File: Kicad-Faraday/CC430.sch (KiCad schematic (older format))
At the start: 33 parts, among them P2 DNP, U1 CC430F6137, U14 0915BM15A0001E, X1 ST3215SB32768H5HPWAA, X2 ABM8G-26.000MHZ-18-D2Y-T

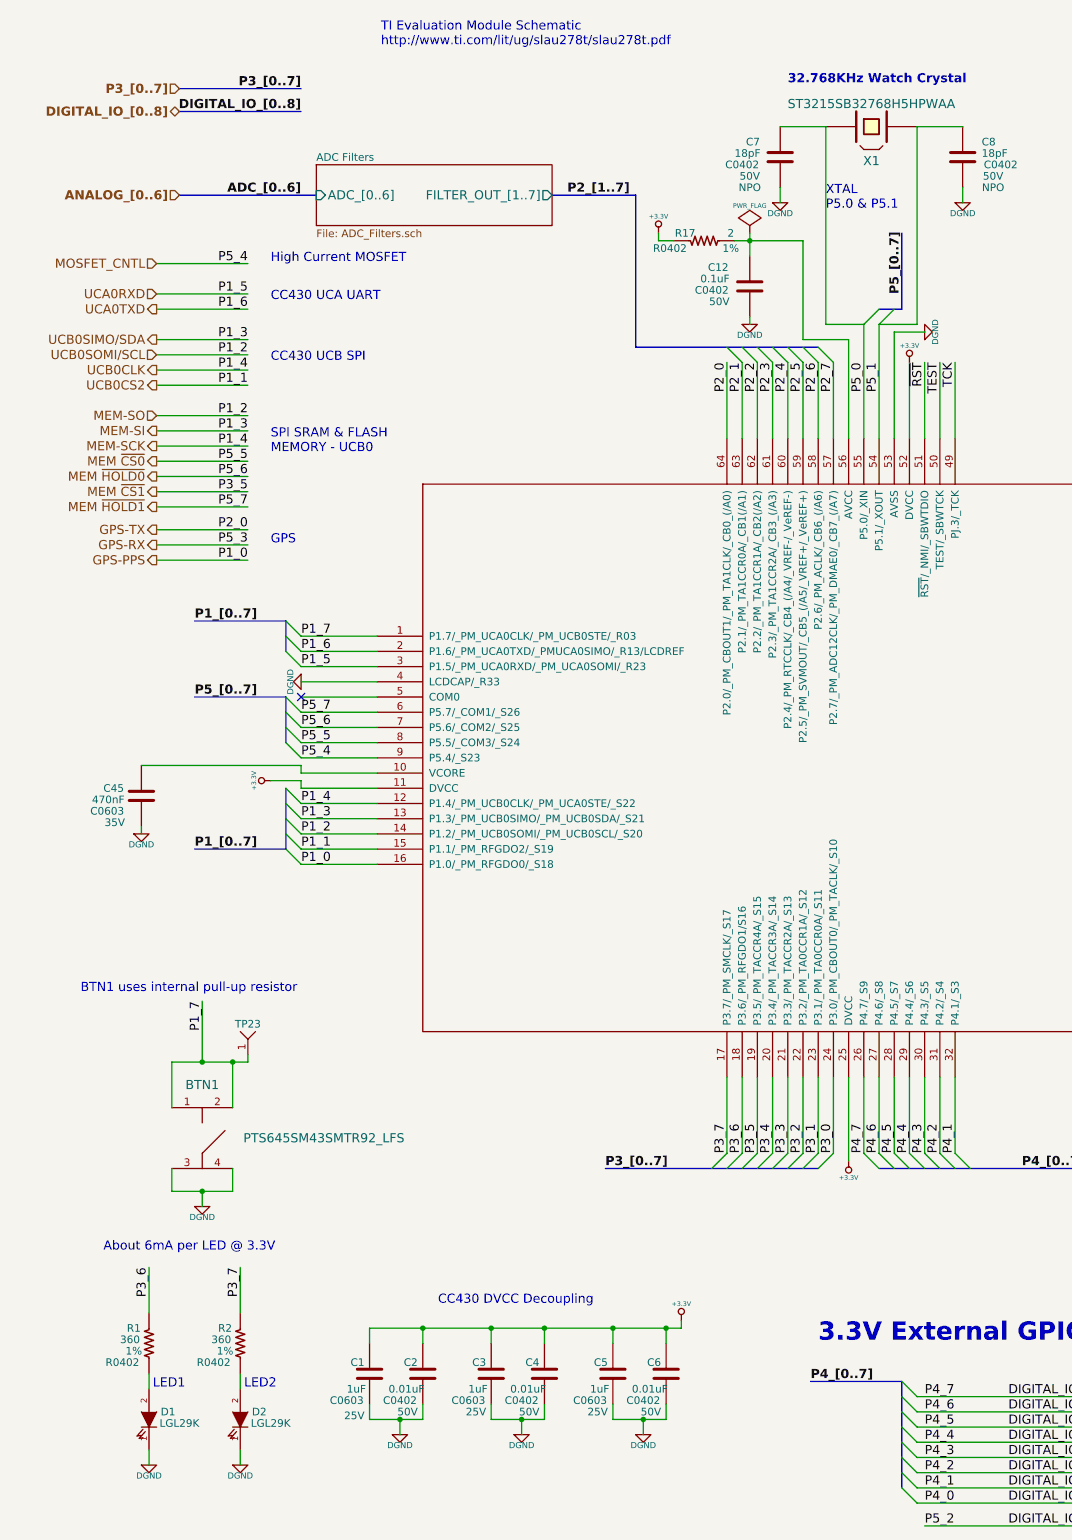
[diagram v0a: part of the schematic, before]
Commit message: Updated BOM .csv and added a REV C BOM Excel document as well as Rev C ICD Excel document. Updated PCB layout file to include P3 and P4 swaps for GD0 changes per GitHub Hardware IT #6.
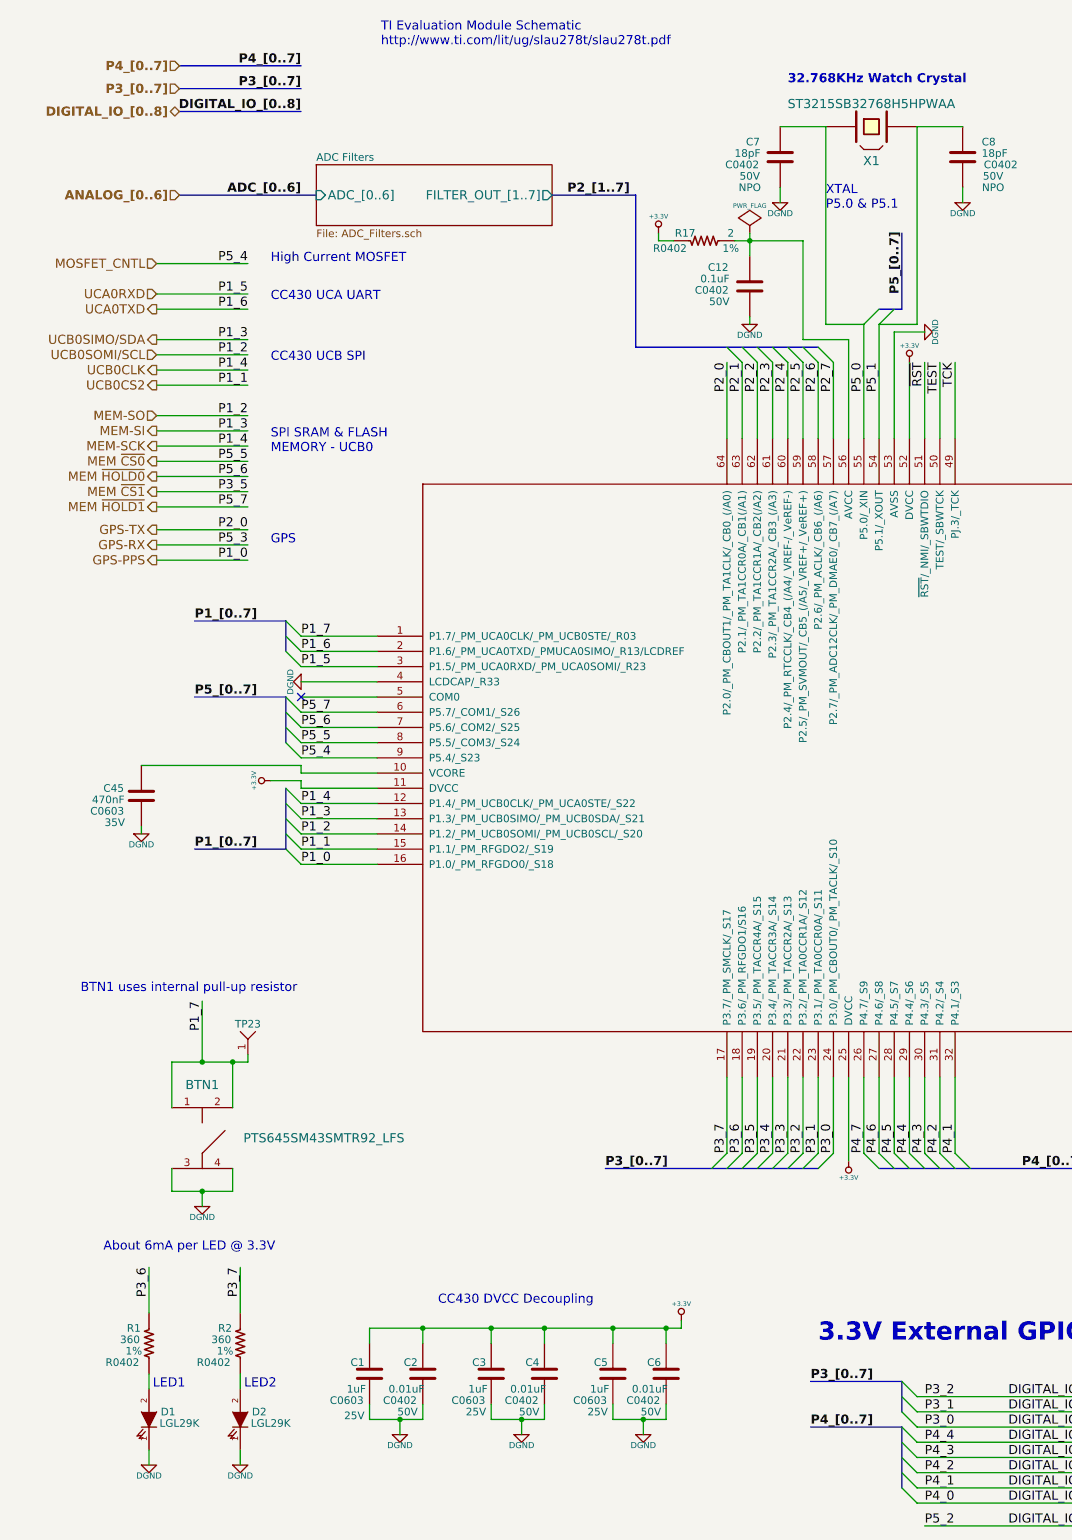
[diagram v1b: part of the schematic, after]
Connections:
- net P3_0 is gone; now on net DIGITAL_IO_2: U1.24 (P3.0/_PM_CBOUT0/_PM_TACLK/_S10)
- net P3_1 is gone; now on net DIGITAL_IO_1: U1.23 (P3.1/_PM_TA0CCR0A/_S11)
- net P3_2 is gone; now on net DIGITAL_IO_0: U1.22 (P3.2/_PM_TA0CCR1A/_S12)
- net DIGITAL_IO_0: no longer U1.26 (P4.7/_S9)
- net DIGITAL_IO_1: no longer U1.27 (P4.6/_S8)
- net DIGITAL_IO_2: no longer U1.28 (P4.5/_S7)
- new net P4_5: U1.28 (P4.5/_S7)
- new net P4_6: U1.27 (P4.6/_S8)
- new net P4_7: U1.26 (P4.7/_S9)
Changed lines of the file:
@@
 	1    0    0    -1
 $EndComp
-Text Label 5600 9450 0    60   ~ 12
+Text Label 5600 9750 0    60   ~ 12
 P4_[0..7]
 Text Notes 5650 9200 0    120  ~ 24
@@
 56 10 04 A1 18 0C 2B 08 82 50 0C 86 15 04 41 28 06 C3 0A 82 20 14 83 61 05 41 10 8A C1 B0 82 20
 08 C5 60 58 41 10 84 62 30 AC 20 08 42 31 FF 0F 83 E1 BA 3C 1C 59 E8 E4 00 00 00 00 49 45 4E 44
-AE 42 60 82 4D $EndBitmap
+AE 42 60 82 17 $EndBitmap
 EndData
 $EndBitmap
@@
 DIGITAL_IO_8
 Wire Bus Line
-	5600 9450 6200 9450
-Wire Bus Line
-	6200 9450 6200 10150
+	5600 9750 6200 9750
 Wire Wire Line
 	6300 9550 7500 9550
@@
 P4_4
 Text Label 6350 9750 0    60   ~ 0
-P4_5
+P3_0
 Text Label 6350 9650 0    60   ~ 0
-P4_6
+P3_1
 Text Label 6350 9550 0    60   ~ 0
-P4_7
+P3_2
 Text Label 1900 3700 2    60   ~ 0
 P5_7
@@
 	0    1    1    0
 $EndComp
+Wire Bus Line
+	6200 9750 6200 10150
+Text Label 5600 9450 0    60   ~ 12
+P3_[0..7]
+Wire Bus Line
+	5600 9450 6200 9450
+Wire Bus Line
+	6200 9450 6200 9650
+Text Label 2250 800  2    60   ~ 12
+P4_[0..7]
+Wire Bus Line
+	1450 800  2250 800
+Text HLabel 1450 800  0    60   Input ~ 12
+P4_[0..7]
 $EndSCHEMATC

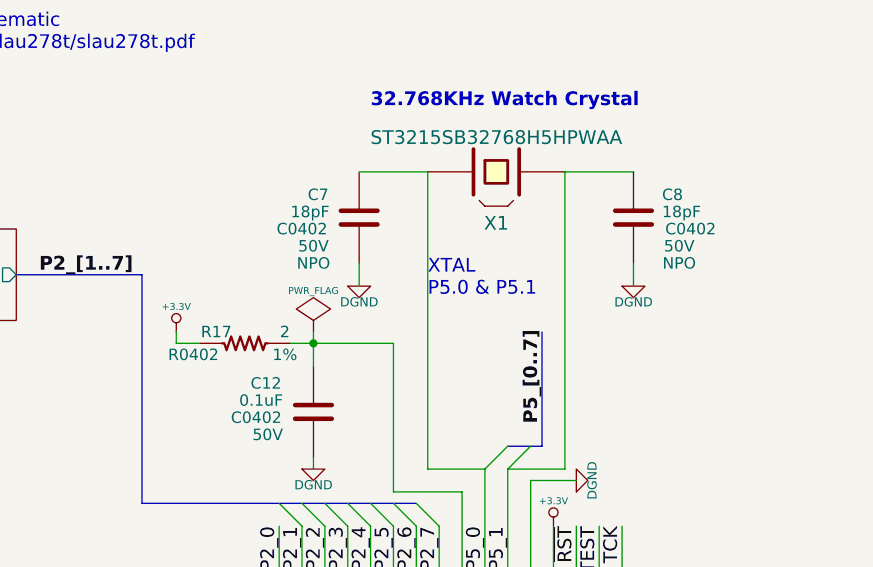
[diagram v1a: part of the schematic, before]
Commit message: Updated per RevD Github Issue comments. Largely removed unnecessary items
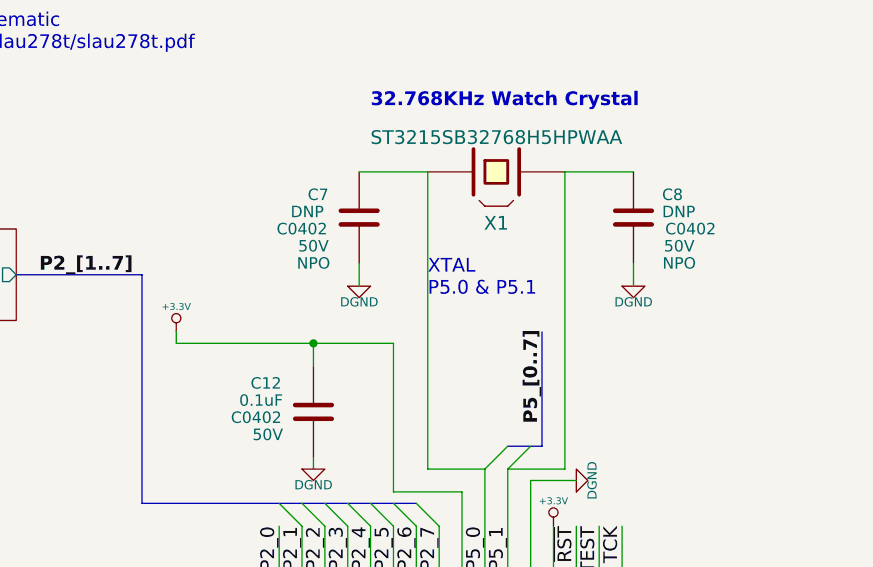
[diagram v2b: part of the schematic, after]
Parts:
- removed R17: 2, R0402, symbol R_US
- C7, C8: value 18pF -> DNP
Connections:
- net +3.3V: now also C12.1, U1.56 (AVCC)
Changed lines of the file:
@@
 Sheet 3 11
 Title "Faraday Wireless Node"
-Date "24 oct 2016"
+Date "10 nov 2016"
 Rev "C"
 Comp "FaradayRF"
@@
 P 6600 1400
 F 0 "C8" H 6725 1500 50  0000 L CNN
-F 1 "18pF" H 6725 1425 50  0000 L CNN
+F 1 "DNP" H 6725 1425 50  0000 L CNN
 F 2 "C0402" H 6850 1350 50  0000 C CNN
 F 3 "" H 6600 1400 60  0000 C CNN
@@
 P 5400 1400
 F 0 "C7" H 5175 1500 50  0000 L CNN
-F 1 "18pF" H 5100 1425 50  0000 L CNN
+F 1 "DNP" H 5100 1425 50  0000 L CNN
 F 2 "C0402" H 5150 1350 50  0000 C CNN
 F 3 "" H 5400 1400 60  0000 C CNN
@@
 NoConn ~ 10700 1950
 $Comp
-L PWR_FLAG #FLG019
+L PWR_FLAG #FLG014
 U 1 1 5416AA97
 P 12250 3400
-F 0 "#FLG019" H 12250 3495 30  0001 C CNN
+F 0 "#FLG014" H 12250 3495 30  0001 C CNN
 F 1 "PWR_FLAG" H 12250 3580 30  0000 C CNN
 F 2 "" H 12250 3400 60  0000 C CNN
@@
 P2_[1..7]
 $Comp
-L +3.3V #PWR020
+L +3.3V #PWR015
 U 1 1 54FE8D21
 P 6250 2750
-F 0 "#PWR020" H 6250 2710 30  0001 C CNN
+F 0 "#PWR015" H 6250 2710 30  0001 C CNN
 F 1 "+3.3V" H 6250 2860 30  0000 C CNN
 F 2 "" H 6250 2750 60  0000 C CNN
@@
 $EndComp
 $Comp
-L +3.3V #PWR021
+L +3.3V #PWR016
 U 1 1 54FE8D46
 P 5850 8000
-F 0 "#PWR021" H 5850 7960 30  0001 C CNN
+F 0 "#PWR016" H 5850 7960 30  0001 C CNN
 F 1 "+3.3V" H 5850 8110 30  0000 C CNN
 F 2 "" H 5850 8000 60  0000 C CNN
@@
 $EndComp
 $Comp
-L +3.3V #PWR022
+L +3.3V #PWR017
 U 1 1 54FE8D77
 P 4750 9050
-F 0 "#PWR022" H 4750 9010 30  0001 C CNN
+F 0 "#PWR017" H 4750 9010 30  0001 C CNN
 F 1 "+3.3V" H 4750 9160 30  0000 C CNN
 F 2 "" H 4750 9050 60  0000 C CNN
@@
 $EndComp
 $Comp
-L +3.3V #PWR023
+L +3.3V #PWR018
 U 1 1 54FE8D9C
 P 2050 5500
-F 0 "#PWR023" H 2050 5460 30  0001 C CNN
+F 0 "#PWR018" H 2050 5460 30  0001 C CNN
 F 1 "+3.3V" H 2050 5610 30  0000 C CNN
 F 2 "" H 2050 5500 60  0000 C CNN
@@
 $EndComp
 $Comp
-L +3.3V #PWR024
+L +3.3V #PWR019
 U 1 1 54FE8DCD
 P 13200 1350
-F 0 "#PWR024" H 13200 1310 30  0001 C CNN
+F 0 "#PWR019" H 13200 1310 30  0001 C CNN
 F 1 "+3.3V" H 13200 1460 30  0000 C CNN
 F 2 "" H 13200 1350 60  0000 C CNN
@@
 $EndComp
 $Comp
-L +3.3V #PWR025
+L +3.3V #PWR020
 U 1 1 54FE8DF2
 P 10050 1350
-F 0 "#PWR025" H 10050 1310 30  0001 C CNN
+F 0 "#PWR020" H 10050 1310 30  0001 C CNN
 F 1 "+3.3V" H 10050 1460 30  0000 C CNN
 F 2 "" H 10050 1350 60  0000 C CNN
@@
 $EndComp
 $Comp
-L +3.3V #PWR026
+L +3.3V #PWR021
 U 1 1 54FE8E1D
 P 4600 1900
-F 0 "#PWR026" H 4600 1860 30  0001 C CNN
+F 0 "#PWR021" H 4600 1860 30  0001 C CNN
 F 1 "+3.3V" H 4600 2010 30  0000 C CNN
 F 2 "" H 4600 1900 60  0000 C CNN
@@
 $EndComp
 $Comp
-L +3.3V #PWR027
+L +3.3V #PWR022
 U 1 1 54FE8E42
 P 13250 3450
-F 0 "#PWR027" H 13250 3410 30  0001 C CNN
+F 0 "#PWR022" H 13250 3410 30  0001 C CNN
 F 1 "+3.3V" H 13250 3560 30  0000 C CNN
 F 2 "" H 13250 3450 60  0000 C CNN
@@
 RF-PWR
 $Comp
-L DGND #PWR028
+L DGND #PWR023
 U 1 1 5518037B
 P 5400 1700
-F 0 "#PWR028" H 5400 1700 40  0001 C CNN
+F 0 "#PWR023" H 5400 1700 40  0001 C CNN
 F 1 "DGND" H 5400 1630 40  0000 C CNN
 F 2 "~" H 5400 1700 60  0000 C CNN
@@
 $EndComp
 $Comp
-L DGND #PWR029
+L DGND #PWR024
 U 1 1 55180450
 P 6600 1700
-F 0 "#PWR029" H 6600 1700 40  0001 C CNN
+F 0 "#PWR024" H 6600 1700 40  0001 C CNN
 F 1 "DGND" H 6600 1630 40  0000 C CNN
 F 2 "~" H 6600 1700 60  0000 C CNN
@@
 $EndComp
 $Comp
-L DGND #PWR030
+L DGND #PWR025
 U 1 1 551805A0
 P 12700 1800
-F 0 "#PWR030" H 12700 1800 40  0001 C CNN
+F 0 "#PWR025" H 12700 1800 40  0001 C CNN
 F 1 "DGND" H 12700 1730 40  0000 C CNN
 F 2 "~" H 12700 1800 60  0000 C CNN
@@
 $EndComp
 $Comp
-L DGND #PWR031
+L DGND #PWR026
 U 1 1 551805D3
 P 13200 2550
-F 0 "#PWR031" H 13200 2550 40  0001 C CNN
+F 0 "#PWR026" H 13200 2550 40  0001 C CNN
 F 1 "DGND" H 13200 2480 40  0000 C CNN
 F 2 "~" H 13200 2550 60  0000 C CNN
@@
 $EndComp
 $Comp
-L DGND #PWR032
+L DGND #PWR027
 U 1 1 55180832
 P 9450 9600
-F 0 "#PWR032" H 9450 9600 40  0001 C CNN
+F 0 "#PWR027" H 9450 9600 40  0001 C CNN
 F 1 "DGND" H 9450 9530 40  0000 C CNN
 F 2 "~" H 9450 9600 60  0000 C CNN
@@
 $EndComp
 $Comp
-L DGND #PWR033
+L DGND #PWR028
 U 1 1 55180838
 P 10050 9600
-F 0 "#PWR033" H 10050 9600 40  0001 C CNN
+F 0 "#PWR028" H 10050 9600 40  0001 C CNN
 F 1 "DGND" H 10050 9530 40  0000 C CNN
 F 2 "~" H 10050 9600 60  0000 C CNN
@@
 $EndComp
 $Comp
-L DGND #PWR034
+L DGND #PWR029
 U 1 1 551809BC
 P 8950 7150
-F 0 "#PWR034" H 8950 7150 40  0001 C CNN
+F 0 "#PWR029" H 8950 7150 40  0001 C CNN
 F 1 "DGND" H 8950 7080 40  0000 C CNN
 F 2 "~" H 8950 7150 60  0000 C CNN
@@
 $EndComp
 $Comp
-L DGND #PWR035
+L DGND #PWR030
 U 1 1 55180BC3
 P 1200 5850
-F 0 "#PWR035" H 1200 5850 40  0001 C CNN
+F 0 "#PWR030" H 1200 5850 40  0001 C CNN
 F 1 "DGND" H 1200 5780 40  0000 C CNN
 F 2 "~" H 1200 5850 60  0000 C CNN
@@
 $EndComp
 $Comp
-L DGND #PWR036
+L DGND #PWR031
 U 1 1 55180C86
 P 1600 8300
-F 0 "#PWR036" H 1600 8300 40  0001 C CNN
+F 0 "#PWR031" H 1600 8300 40  0001 C CNN
 F 1 "DGND" H 1600 8230 40  0000 C CNN
 F 2 "~" H 1600 8300 60  0000 C CNN
@@
 $EndComp
 $Comp
-L DGND #PWR037
+L DGND #PWR032
 U 1 1 55180D37
 P 1850 10000
-F 0 "#PWR037" H 1850 10000 40  0001 C CNN
+F 0 "#PWR032" H 1850 10000 40  0001 C CNN
 F 1 "DGND" H 1850 9930 40  0000 C CNN
 F 2 "~" H 1850 10000 60  0000 C CNN
@@
 $EndComp
 $Comp
-L DGND #PWR038
+L DGND #PWR033
 U 1 1 55180D58
 P 1250 10000
-F 0 "#PWR038" H 1250 10000 40  0001 C CNN
+F 0 "#PWR033" H 1250 10000 40  0001 C CNN
 F 1 "DGND" H 1250 9930 40  0000 C CNN
 F 2 "~" H 1250 10000 60  0000 C CNN
@@
 $EndComp
 $Comp
-L DGND #PWR039
+L DGND #PWR034
 U 1 1 55180ED9
 P 2900 9800
-F 0 "#PWR039" H 2900 9800 40  0001 C CNN
+F 0 "#PWR034" H 2900 9800 40  0001 C CNN
 F 1 "DGND" H 2900 9730 40  0000 C CNN
 F 2 "~" H 2900 9800 60  0000 C CNN
@@
 $EndComp
 $Comp
-L DGND #PWR040
+L DGND #PWR035
 U 1 1 55180EE6
 P 3700 9800
-F 0 "#PWR040" H 3700 9800 40  0001 C CNN
+F 0 "#PWR035" H 3700 9800 40  0001 C CNN
 F 1 "DGND" H 3700 9730 40  0000 C CNN
 F 2 "~" H 3700 9800 60  0000 C CNN
@@
 $EndComp
 $Comp
-L DGND #PWR041
+L DGND #PWR036
 U 1 1 55180EEC
 P 4500 9800
-F 0 "#PWR041" H 4500 9800 40  0001 C CNN
+F 0 "#PWR036" H 4500 9800 40  0001 C CNN
 F 1 "DGND" H 4500 9730 40  0000 C CNN
 F 2 "~" H 4500 9800 60  0000 C CNN
@@
 $EndComp
 $Comp
-L DGND #PWR042
+L DGND #PWR037
 U 1 1 55183E70
 P 9750 9000
-F 0 "#PWR042" H 9750 9000 40  0001 C CNN
+F 0 "#PWR037" H 9750 9000 40  0001 C CNN
 F 1 "DGND" H 9750 8930 40  0000 C CNN
 F 2 "~" H 9750 9000 60  0000 C CNN
@@
 32.768KHz Watch Crystal
 $Comp
-L DGND #PWR043
+L DGND #PWR038
 U 1 1 55A542F7
 P 11450 4250
-F 0 "#PWR043" H 11450 4250 40  0001 C CNN
+F 0 "#PWR038" H 11450 4250 40  0001 C CNN
 F 1 "DGND" H 11450 4180 40  0000 C CNN
 F 2 "~" H 11450 4250 60  0000 C CNN
@@
 $EndComp
 $Comp
-L DGND #PWR044
+L DGND #PWR039
 U 1 1 55A543D5
 P 10450 4250
-F 0 "#PWR044" H 10450 4250 40  0001 C CNN
+F 0 "#PWR039" H 10450 4250 40  0001 C CNN
 F 1 "DGND" H 10450 4180 40  0000 C CNN
 F 2 "~" H 10450 4250 60  0000 C CNN
@@
 $EndComp
 $Comp
-L DGND #PWR045
+L DGND #PWR040
 U 1 1 55A54975
 P 9850 5000
-F 0 "#PWR045" H 9850 5000 40  0001 C CNN
+F 0 "#PWR040" H 9850 5000 40  0001 C CNN
 F 1 "DGND" H 9850 4930 40  0000 C CNN
 F 2 "~" H 9850 5000 60  0000 C CNN
@@
 $EndComp
 $Comp
-L DGND #PWR046
+L DGND #PWR041
 U 1 1 55BDE204
 P 6350 2550
-F 0 "#PWR046" H 6350 2550 40  0001 C CNN
+F 0 "#PWR041" H 6350 2550 40  0001 C CNN
 F 1 "DGND" H 6350 2480 40  0000 C CNN
 F 2 "~" H 6350 2550 60  0000 C CNN
@@
 $EndComp
 $Comp
-L DGND #PWR047
+L DGND #PWR042
 U 1 1 55BDE222
 P 5200 2500
-F 0 "#PWR047" H 5200 2500 40  0001 C CNN
+F 0 "#PWR042" H 5200 2500 40  0001 C CNN
 F 1 "DGND" H 5200 2430 40  0000 C CNN
 F 2 "~" H 5200 2500 60  0000 C CNN
@@
 	1    0    0    -1
 $EndComp
-$Comp
-L R_US R17
-U 1 1 55BF5F34
-P 4900 1950
-F 0 "R17" V 4950 2075 50  0000 C CNN
-F 1 "2" V 4950 1775 50  0000 C CNN
-F 2 "R0402" V 4850 2175 50  0000 C CNN
-F 3 "" H 4900 1950 60  0000 C CNN
-F 4 "1%" V 4850 1775 50  0000 C CNN "Tolerance"
-	1    4900 1950
-	0    -1   -1   0
-$EndComp
 Text Notes 12450 3700 0    60   ~ 0
 Ferrite Bead
-$Comp
-L PWR_FLAG #FLG048
-U 1 1 55C2C142
-P 5200 1900
-F 0 "#FLG048" H 5200 1995 30  0001 C CNN
-F 1 "PWR_FLAG" H 5200 2080 30  0000 C CNN
-F 2 "" H 5200 1900 60  0000 C CNN
-F 3 "" H 5200 1900 60  0000 C CNN
-	1    5200 1900
-	1    0    0    -1
-$EndComp
 $Bitmap
 Pos 1300 6400
@@
 56 10 04 A1 18 0C 2B 08 82 50 0C 86 15 04 41 28 06 C3 0A 82 20 14 83 61 05 41 10 8A C1 B0 82 20
 08 C5 60 58 41 10 84 62 30 AC 20 08 42 31 FF 0F 83 E1 BA 3C 1C 59 E8 E4 00 00 00 00 49 45 4E 44
-AE 42 60 82 17 $EndBitmap
+AE 42 60 82 33 $EndBitmap
 EndData
 $EndBitmap
 $Comp
-L DGND #PWR049
+L DGND #PWR043
 U 1 1 55C4A709
 P 2250 4850
-F 0 "#PWR049" H 2250 4850 40  0001 C CNN
+F 0 "#PWR043" H 2250 4850 40  0001 C CNN
 F 1 "DGND" H 2250 4780 40  0000 C CNN
 F 2 "~" H 2250 4850 60  0000 C CNN
@@
 Connection ~ 5200 1950
 Wire Wire Line
-	5100 1950 5550 1950
-Wire Wire Line
-	4600 1950 4700 1950
+	4600 1950 5550 1950
 Wire Wire Line
 	4600 1900 4600 1950
@@
 Wire Wire Line
 	5200 2450 5200 2500
-Wire Wire Line
-	5200 1900 5200 2050
 Connection ~ 1600 7350
 Wire Wire Line
@@
 Connection ~ 10300 1650
 $Comp
-L DGND #PWR050
+L DGND #PWR044
 U 1 1 578D5F78
 P 10300 2550
-F 0 "#PWR050" H 10300 2550 40  0001 C CNN
+F 0 "#PWR044" H 10300 2550 40  0001 C CNN
 F 1 "DGND" H 10300 2480 40  0000 C CNN
 F 2 "~" H 10300 2550 60  0000 C CNN
@@
 	10350 5750 10400 5750
 $Comp
-L DGND #PWR051
+L DGND #PWR045
 U 1 1 57944E95
 P 11700 6350
-F 0 "#PWR051" H 11700 6350 40  0001 C CNN
+F 0 "#PWR045" H 11700 6350 40  0001 C CNN
 F 1 "DGND" H 11700 6280 40  0000 C CNN
 F 2 "~" H 11700 6350 60  0000 C CNN
@@
 Text HLabel 1450 800  0    60   Input ~ 12
 P4_[0..7]
+Wire Wire Line
+	5200 1950 5200 2050
 $EndSCHEMATC

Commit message: Saving current RevD, need ot export BOM
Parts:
- BTN1: value PTS645SM43SMTR92_LFS -> DNP
- C2, C4, C6: value 0.01uF -> 0.1uF
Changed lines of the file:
@@
 P 3050 9400
 F 0 "C2" H 2925 9475 50  0000 L CNN
-F 1 "0.01uF" H 2825 9300 50  0000 L CNN
+F 1 "0.1uF" H 2825 9300 50  0000 L CNN
 F 2 "C0402" H 2900 9225 50  0000 C CNN
 F 3 "" H 3050 9400 60  0000 C CNN
@@
 P 3850 9400
 F 0 "C4" H 3725 9475 50  0000 L CNN
-F 1 "0.01uF" H 3625 9300 50  0000 L CNN
+F 1 "0.1uF" H 3625 9300 50  0000 L CNN
 F 2 "C0402" H 3700 9225 50  0000 C CNN
 F 3 "" H 3850 9400 60  0000 C CNN
@@
 P 4650 9400
 F 0 "C6" H 4525 9475 50  0000 L CNN
-F 1 "0.01uF" H 4425 9300 50  0000 L CNN
+F 1 "0.1uF" H 4425 9300 50  0000 L CNN
 F 2 "C0402" H 4500 9225 50  0000 C CNN
 F 3 "" H 4650 9400 60  0000 C CNN
@@
 P 1600 7850
 F 0 "BTN1" H 1600 8200 60  0000 C CNN
-F 1 "PTS645SM43SMTR92_LFS" H 2400 7850 60  0000 C CNN
+F 1 "DNP" H 1600 7550 60  0000 C CNN
 F 2 "PTS645-SMD" H 1600 7850 60  0001 C CNN
 F 3 "" H 1600 7850 60  0000 C CNN
